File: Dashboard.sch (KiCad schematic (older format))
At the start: 24 parts, among them J24 ExtraGPIO_Conn, J25 UART_TP, J8 JTAG, SW10 RESET, U7 STM32F413RHTx, Y1 Crystal

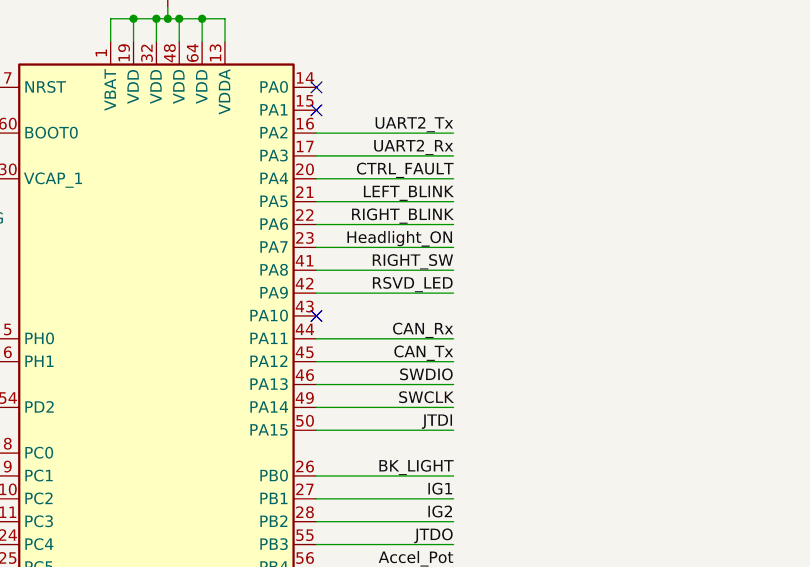
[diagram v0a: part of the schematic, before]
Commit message: Adds components for the shift register and lays out modularized components
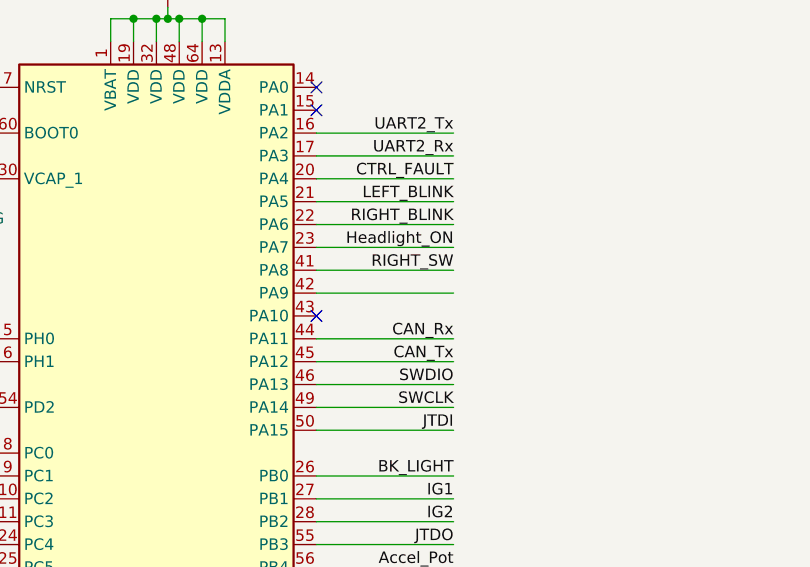
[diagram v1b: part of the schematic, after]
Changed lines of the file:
@@
 Text Label 9600 5150 2    50   ~ 0
 CTRL_FAULT
-Text Label 9600 5650 2    50   ~ 0
-RSVD_LED
 Wire Wire Line
 	9600 7750 9000 7750
@@
 Wire Wire Line
 	7450 5150 7600 5150
+Text Label 2950 7550 0    50   ~ 0
+A_PRCHG
+Text Label 2950 7450 0    50   ~ 0
+A_CNCTR
+Text Label 2950 7300 0    50   ~ 0
+M_PRCHG
+Text Label 2950 7200 0    50   ~ 0
+M_CNCTR
+Wire Wire Line
+	2700 7550 2950 7550
+Wire Wire Line
+	2700 7450 2950 7450
+Wire Wire Line
+	2700 7300 2950 7300
+Wire Wire Line
+	2700 7200 2950 7200
+Text Label 9600 5050 2    50   ~ 0
+UART2_Rx
+Text Label 9600 4950 2    50   ~ 0
+UART2_Tx
+Wire Wire Line
+	7600 6550 7000 6550
+Text Label 7000 6550 0    50   ~ 0
+M_PRCHG
+Wire Wire Line
+	7000 6450 7600 6450
+Text Label 7000 6450 0    50   ~ 0
+A_CNCTR
+Wire Wire Line
+	7600 6350 7000 6350
+Text Label 7000 6350 0    50   ~ 0
+A_PRCHG
+Text Label 7000 6150 0    50   ~ 0
+PD2
+Text Label 7000 7350 0    50   ~ 0
+PC10
+Text Label 7000 7450 0    50   ~ 0
+PC11
+Text Label 7000 7550 0    50   ~ 0
+PC12
+NoConn ~ 9000 4750
+NoConn ~ 9000 4850
+NoConn ~ 9000 5750
+NoConn ~ 9000 7250
+NoConn ~ 9000 7350
+Wire Wire Line
+	11500 6350 11950 6350
+Wire Wire Line
+	11500 6250 11950 6250
+Wire Wire Line
+	11500 6150 11950 6150
+Text Label 11500 6350 0    50   ~ 0
+PC10
+Text Label 11500 6150 0    50   ~ 0
+PC12
+Text Label 11500 6250 0    50   ~ 0
+PC11
+Text Label 12900 6350 2    50   ~ 0
+PC13
+Wire Wire Line
+	11500 6050 11950 6050
+Wire Wire Line
+	12900 6350 12450 6350
+Wire Wire Line
+	12900 6250 12450 6250
+Wire Wire Line
+	12900 6150 12450 6150
+Text Label 12900 6250 2    50   ~ 0
+PC14
+Text Label 11500 6050 0    50   ~ 0
+PD2
+NoConn ~ 12450 6050
+Text Label 5300 10150 0    50   ~ 0
+UART2_Tx
+Wire Wire Line
+	5050 10150 5300 10150
+Wire Wire Line
+	5050 10050 5300 10050
+Text Label 5300 10050 0    50   ~ 0
+UART2_Rx
+Text Label 5300 9900 0    50   ~ 0
+MOSI
+Text Label 5300 9800 0    50   ~ 0
+MISO
+Text Label 5300 9700 0    50   ~ 0
+SCK
+Text Label 5300 9600 0    50   ~ 0
+CS
+Wire Wire Line
+	5050 9900 5300 9900
+Wire Wire Line
+	5050 9800 5300 9800
+Wire Wire Line
+	5050 9700 5300 9700
+Wire Wire Line
+	5050 9600 5300 9600
 $Sheet
 S 3900 9450 1150 900
@@
 F7 "UART2_Tx" I R 5050 10150 50
 $EndSheet
+Text Label 2950 10200 0    50   ~ 0
+MOSI
+Text Label 2950 10100 0    50   ~ 0
+MISO
+Text Label 2950 10000 0    50   ~ 0
+SCK
+Text Label 2950 9900 0    50   ~ 0
+CS
+Text Label 2950 9750 0    50   ~ 0
+RIGHT_SW
+Text Label 2950 9650 0    50   ~ 0
+LEFT_SW
+Text Label 2950 9550 0    50   ~ 0
+Headlight_SW
+Text Label 2950 9450 0    50   ~ 0
+FR_SW
+Text Label 2950 9350 0    50   ~ 0
+HZD_SW
+Text Label 2950 9250 0    50   ~ 0
+CRUZ_EN
+Text Label 2950 9150 0    50   ~ 0
+CRUZ_ST
+Text Label 2950 8900 0    50   ~ 0
+BPS_PWR
+Text Label 2950 8500 0    50   ~ 0
+LEFT_BLINK
+Text Label 2950 8800 0    50   ~ 0
+BPS_FAULT
+Text Label 2950 8200 0    50   ~ 0
+A_CNCTR
+Text Label 2950 8700 0    50   ~ 0
+Headlight_ON
+Text Label 2950 8600 0    50   ~ 0
+RIGHT_BLINK
+Text Label 2950 8400 0    50   ~ 0
+CTRL_FAULT
+Text Label 2950 9000 0    50   ~ 0
+RSVD_LED
+Wire Wire Line
+	2700 9750 2950 9750
+Wire Wire Line
+	2700 9650 2950 9650
+Wire Wire Line
+	2700 9550 2950 9550
+Wire Wire Line
+	2700 10200 2950 10200
+Wire Wire Line
+	2700 10100 2950 10100
+Wire Wire Line
+	2700 10000 2950 10000
+Wire Wire Line
+	2700 9900 2950 9900
+Wire Wire Line
+	2700 9450 2950 9450
+Wire Wire Line
+	2700 9350 2950 9350
+Wire Wire Line
+	2700 9250 2950 9250
+Wire Wire Line
+	2700 9150 2950 9150
+Wire Wire Line
+	2700 9000 2950 9000
+Wire Wire Line
+	2700 8900 2950 8900
+Wire Wire Line
+	2700 8800 2950 8800
+Wire Wire Line
+	2700 8700 2950 8700
+Wire Wire Line
+	2700 8600 2950 8600
+Wire Wire Line
+	2700 8500 2950 8500
+Wire Wire Line
+	2700 8400 2950 8400
+Wire Wire Line
+	2700 8200 2950 8200
+Wire Wire Line
+	2700 8300 2950 8300
+Text Label 2950 8300 0    50   ~ 0
+M_CNCTR
 $Sheet
 S 1550 8050 1150 2350
@@
 F21 "MOSI" O R 2700 10200 50
 $EndSheet
-Text Label 2950 7550 0    50   ~ 0
-A_PRCHG
-Text Label 2950 7450 0    50   ~ 0
-A_CNCTR
-Text Label 2950 7300 0    50   ~ 0
-M_PRCHG
-Text Label 2950 7200 0    50   ~ 0
-M_CNCTR
-Wire Wire Line
-	2700 7550 2950 7550
-Wire Wire Line
-	2700 7450 2950 7450
-Wire Wire Line
-	2700 7300 2950 7300
-Wire Wire Line
-	2700 7200 2950 7200
-Text Label 2950 8300 0    50   ~ 0
-M_CNCTR
-Wire Wire Line
-	2700 8300 2950 8300
-Wire Wire Line
-	2700 8200 2950 8200
-Wire Wire Line
-	2700 8400 2950 8400
-Wire Wire Line
-	2700 8500 2950 8500
-Wire Wire Line
-	2700 8600 2950 8600
-Wire Wire Line
-	2700 8700 2950 8700
-Wire Wire Line
-	2700 8800 2950 8800
-Wire Wire Line
-	2700 8900 2950 8900
-Wire Wire Line
-	2700 9000 2950 9000
-Wire Wire Line
-	2700 9150 2950 9150
-Wire Wire Line
-	2700 9250 2950 9250
-Wire Wire Line
-	2700 9350 2950 9350
-Wire Wire Line
-	2700 9450 2950 9450
-Wire Wire Line
-	2700 9900 2950 9900
-Wire Wire Line
-	2700 10000 2950 10000
-Wire Wire Line
-	2700 10100 2950 10100
-Wire Wire Line
-	2700 10200 2950 10200
-Wire Wire Line
-	2700 9550 2950 9550
-Wire Wire Line
-	2700 9650 2950 9650
-Wire Wire Line
-	2700 9750 2950 9750
-Text Label 2950 9000 0    50   ~ 0
-RSVD_LED
-Text Label 2950 8400 0    50   ~ 0
-CTRL_FAULT
-Text Label 2950 8600 0    50   ~ 0
-RIGHT_BLINK
-Text Label 2950 8700 0    50   ~ 0
-Headlight_ON
-Text Label 2950 8200 0    50   ~ 0
-A_CNCTR
-Text Label 2950 8800 0    50   ~ 0
-BPS_FAULT
-Text Label 2950 8500 0    50   ~ 0
-LEFT_BLINK
-Text Label 2950 8900 0    50   ~ 0
-BPS_PWR
-Text Label 2950 9150 0    50   ~ 0
-CRUZ_ST
-Text Label 2950 9250 0    50   ~ 0
-CRUZ_EN
-Text Label 2950 9350 0    50   ~ 0
-HZD_SW
-Text Label 2950 9450 0    50   ~ 0
-FR_SW
-Text Label 2950 9550 0    50   ~ 0
-Headlight_SW
-Text Label 2950 9650 0    50   ~ 0
-LEFT_SW
-Text Label 2950 9750 0    50   ~ 0
-RIGHT_SW
-Text Label 2950 9900 0    50   ~ 0
-CS
-Text Label 2950 10000 0    50   ~ 0
-SCK
-Text Label 2950 10100 0    50   ~ 0
-MISO
-Text Label 2950 10200 0    50   ~ 0
-MOSI
-Text Label 9600 5050 2    50   ~ 0
-UART2_Rx
-Text Label 9600 4950 2    50   ~ 0
-UART2_Tx
-Wire Wire Line
-	5050 9600 5300 9600
-Wire Wire Line
-	5050 9700 5300 9700
-Wire Wire Line
-	5050 9800 5300 9800
-Wire Wire Line
-	5050 9900 5300 9900
-Text Label 5300 9600 0    50   ~ 0
-CS
-Text Label 5300 9700 0    50   ~ 0
-SCK
-Text Label 5300 9800 0    50   ~ 0
-MISO
-Text Label 5300 9900 0    50   ~ 0
-MOSI
-Text Label 5300 10050 0    50   ~ 0
-UART2_Rx
-Wire Wire Line
-	5050 10050 5300 10050
-Wire Wire Line
-	5050 10150 5300 10150
-Text Label 5300 10150 0    50   ~ 0
-UART2_Tx
-Wire Wire Line
-	7600 6550 7000 6550
-Text Label 7000 6550 0    50   ~ 0
-M_PRCHG
-Wire Wire Line
-	7000 6450 7600 6450
-Text Label 7000 6450 0    50   ~ 0
-A_CNCTR
-Wire Wire Line
-	7600 6350 7000 6350
-Text Label 7000 6350 0    50   ~ 0
-A_PRCHG
-Text Label 7000 6150 0    50   ~ 0
-PD2
-Text Label 7000 7350 0    50   ~ 0
-PC10
-Text Label 7000 7450 0    50   ~ 0
-PC11
-Text Label 7000 7550 0    50   ~ 0
-PC12
-NoConn ~ 9000 4750
-NoConn ~ 9000 4850
-NoConn ~ 9000 5750
-NoConn ~ 9000 7250
-NoConn ~ 9000 7350
-Wire Wire Line
-	11500 6350 11950 6350
-Wire Wire Line
-	11500 6250 11950 6250
-Wire Wire Line
-	11500 6150 11950 6150
-Text Label 11500 6350 0    50   ~ 0
-PC10
-Text Label 11500 6150 0    50   ~ 0
-PC12
-Text Label 11500 6250 0    50   ~ 0
-PC11
-Text Label 12900 6350 2    50   ~ 0
-PC13
-Wire Wire Line
-	11500 6050 11950 6050
-Wire Wire Line
-	12900 6350 12450 6350
-Wire Wire Line
-	12900 6250 12450 6250
-Wire Wire Line
-	12900 6150 12450 6150
-Text Label 12900 6250 2    50   ~ 0
-PC14
 Text Label 12900 6150 2    50   ~ 0
 PC15
-Text Label 11500 6050 0    50   ~ 0
-PD2
-NoConn ~ 12450 6050
 $EndSCHEMATC

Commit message: Lays out PCB for Controls leader board
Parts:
- LOGO1: footprint UTSVT_Special:Hallock_Image_Small -> UTSVT_Special:Hallock_Image
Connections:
- net labels added: CLK, PB4, PB5, PB6, PB7
- net labels removed: BPS_FAULT, CRUZ_EN, CRUZ_ST, CTRL_FAULT, FR_SW, HZD_SW, Headlight_SW, LEFT_SW, PC10, PC11, PC12, PD2, RIGHT_SW, RSVD_LED, SCK
- wire segments 190 -> 164
- no-connect marks 6 -> 12

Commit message: Adds labels to some connectors and edits layout to meet 0,2mm pad to trace clearance
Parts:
- J25: footprint Connector_PinHeader_2.54mm:PinHeader_1x02_P2.54mm_Vertical -> Connector_PinHeader_2.54mm:PinHeader_1x03_P2.54mm_Vertical; symbol Connector_Generic:Conn_01x02 -> Connector_Generic:Conn_01x03
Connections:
- wire segments 164 -> 168
- no-connect marks 12 -> 11
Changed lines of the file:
@@
 L Connector_Generic:Conn_02x04_Odd_Even J24
 U 1 1 600A02F6
-P 12150 6150
-F 0 "J24" H 12300 5850 50  0000 L CNN
-F 1 "ExtraGPIO_Conn" H 12300 5750 50  0000 L CNN
-F 2 "Connector_PinHeader_2.54mm:PinHeader_2x04_P2.54mm_Vertical" H 12150 6150 50  0001 C CNN
-F 3 "~" H 12150 6150 50  0001 C CNN
-	1    12150 6150
-	1    0    0    -1
+P 12250 6150
+F 0 "J24" H 12400 5850 50  0000 L CNN
+F 1 "ExtraGPIO_Conn" H 12400 5750 50  0000 L CNN
+F 2 "Connector_PinHeader_2.54mm:PinHeader_2x04_P2.54mm_Vertical" H 12250 6150 50  0001 C CNN
+F 3 "~" H 12250 6150 50  0001 C CNN
+	1    12250 6150
+	-1   0    0    -1
 $EndComp
 $Sheet
@@
 	2700 4050 2950 4050
 $Comp
-L Connector_Generic:Conn_01x02 J?
+L Connector_Generic:Conn_01x03 J?
 U 1 1 5FBDC250
 P 12150 6850
@@
 F 0 "J25" H 12300 6850 50  0000 C CNN
 F 1 "UART_TP" H 12400 6750 50  0000 C CNN
-F 2 "Connector_PinHeader_2.54mm:PinHeader_1x02_P2.54mm_Vertical" H 12150 6850 50  0001 C CNN
+F 2 "Connector_PinHeader_2.54mm:PinHeader_1x03_P2.54mm_Vertical" H 12150 6850 50  0001 C CNN
 F 3 "~" H 12150 6850 50  0001 C CNN
 	1    12150 6850
@@
 Wire Wire Line
 	11500 6150 11950 6150
-Text Label 11500 6350 0    50   ~ 0
-PB4
-Text Label 11500 6150 0    50   ~ 0
-PB6
-Text Label 11500 6250 0    50   ~ 0
-PB5
-Text Label 12900 6350 2    50   ~ 0
+Text Label 12900 6150 2    50   ~ 0
 PC13
 Wire Wire Line
@@
 Text Label 12900 6250 2    50   ~ 0
 PC14
-Text Label 11500 6050 0    50   ~ 0
-PB7
-NoConn ~ 12450 6050
 Text Label 2950 8750 0    50   ~ 0
 UART3_Tx
@@
 F7 "UART_Tx" I R 2700 8750 50
 $EndSheet
-Text Label 12900 6150 2    50   ~ 0
+Text Label 12900 6350 2    50   ~ 0
 PC15
 Wire Wire Line
@@
 Text Label 11500 6950 0    50   ~ 0
 UART2_Rx
+$Comp
+L power:GND #PWR0127
+U 1 1 5F80136C
+P 12500 6450
+F 0 "#PWR0127" H 12500 6200 50  0001 C CNN
+F 1 "GND" H 12505 6277 50  0000 C CNN
+F 2 "" H 12500 6450 50  0001 C CNN
+F 3 "" H 12500 6450 50  0001 C CNN
+	1    12500 6450
+	1    0    0    -1
+$EndComp
+Wire Wire Line
+	12500 6450 12500 6050
+Wire Wire Line
+	12500 6050 12450 6050
+$Comp
+L power:GND #PWR0128
+U 1 1 5F80BFC1
+P 11900 7050
+F 0 "#PWR0128" H 11900 6800 50  0001 C CNN
+F 1 "GND" H 11905 6877 50  0000 C CNN
+F 2 "" H 11900 7050 50  0001 C CNN
+F 3 "" H 11900 7050 50  0001 C CNN
+	1    11900 7050
+	1    0    0    -1
+$EndComp
+Wire Wire Line
+	11900 7050 11900 6750
+Wire Wire Line
+	11900 6750 11950 6750
+Text Label 11500 6350 0    50   ~ 0
+PB7
+Text Label 11500 6250 0    50   ~ 0
+PB6
+Text Label 11500 6150 0    50   ~ 0
+PB5
+Text Label 11500 6050 0    50   ~ 0
+PB4
 $EndSCHEMATC

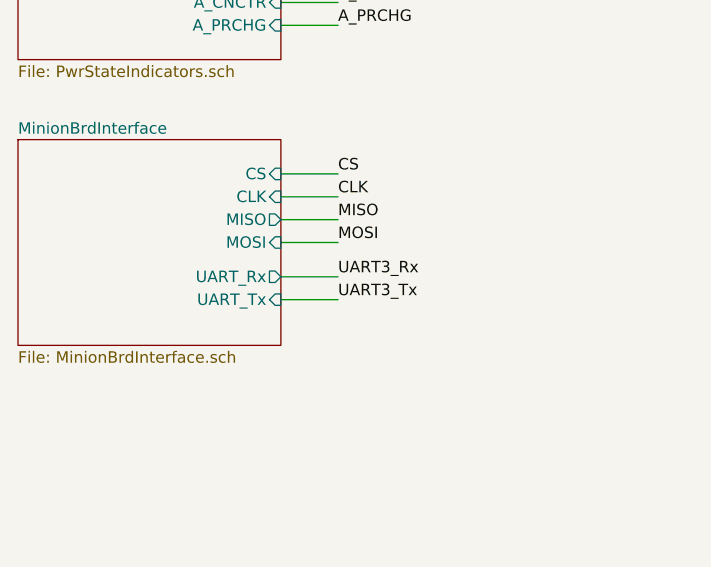
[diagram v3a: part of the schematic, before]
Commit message: Adds BPSPWR as a connection to the minion board and then fixes labels
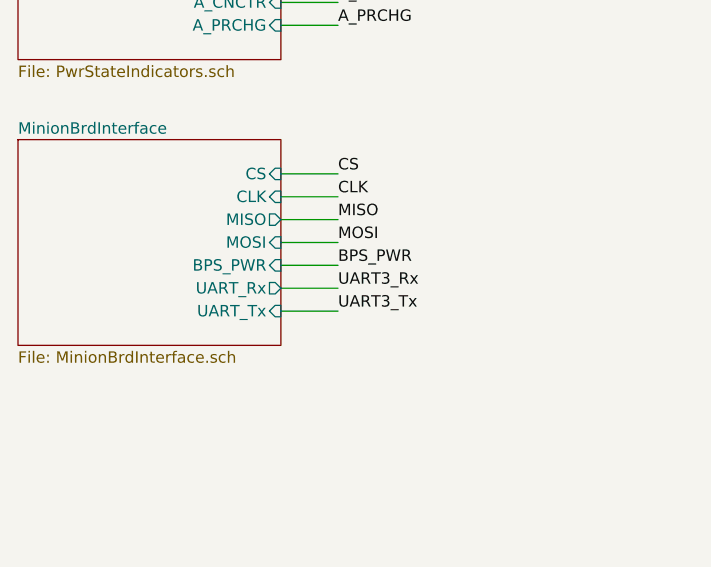
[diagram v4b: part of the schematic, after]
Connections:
- wire segments 168 -> 169
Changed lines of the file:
@@
 Text Label 12900 6250 2    50   ~ 0
 PC14
-Text Label 2950 8750 0    50   ~ 0
+Text Label 2950 8800 0    50   ~ 0
 UART3_Tx
 Wire Wire Line
-	2700 8750 2950 8750
+	2700 8800 2950 8800
 Wire Wire Line
-	2700 8650 2950 8650
-Text Label 2950 8650 0    50   ~ 0
+	2700 8700 2950 8700
+Text Label 2950 8700 0    50   ~ 0
 UART3_Rx
 Text Label 2950 8500 0    50   ~ 0
@@
 F4 "CLK" I R 2700 8300 50
 F5 "CS" I R 2700 8200 50
-F6 "UART_Rx" O R 2700 8650 50
-F7 "UART_Tx" I R 2700 8750 50
+F6 "UART_Rx" O R 2700 8700 50
+F7 "UART_Tx" I R 2700 8800 50
+F8 "BPS_PWR" I R 2700 8600 50
 $EndSheet
 Text Label 12900 6350 2    50   ~ 0
@@
 Text Label 11500 6050 0    50   ~ 0
 PB4
+Text Label 2950 8600 0    50   ~ 0
+BPS_PWR
+Wire Wire Line
+	2950 8600 2700 8600
 $EndSCHEMATC
